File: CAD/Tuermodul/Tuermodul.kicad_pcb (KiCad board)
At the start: 2 copper layers, 160 x 100 mm, 95 parts, among them J101 Conn_02x16_Counter_Clockwise, Q201 Q_NPN_CBE, Q202 Q_NPN_CBE, Q203 Q_NPN_CBE, Q204 Q_NPN_CBE, Q205 Q_NPN_CBE, Q206 Q_NPN_CBE, Q207 Q_NPN_CBE, Q208 Q_NPN_CBE, Q209 Q_PMOS_GDS, Q210 Q_PMOS_GDS, Q211 Q_PMOS_GDS, Q212 Q_PMOS_GDS, Q213 Q_NPN_CBE, U101 93LC46B, U102 74HC595, U103 FT4232H, U104 MCP1825S, Y101 12MHz

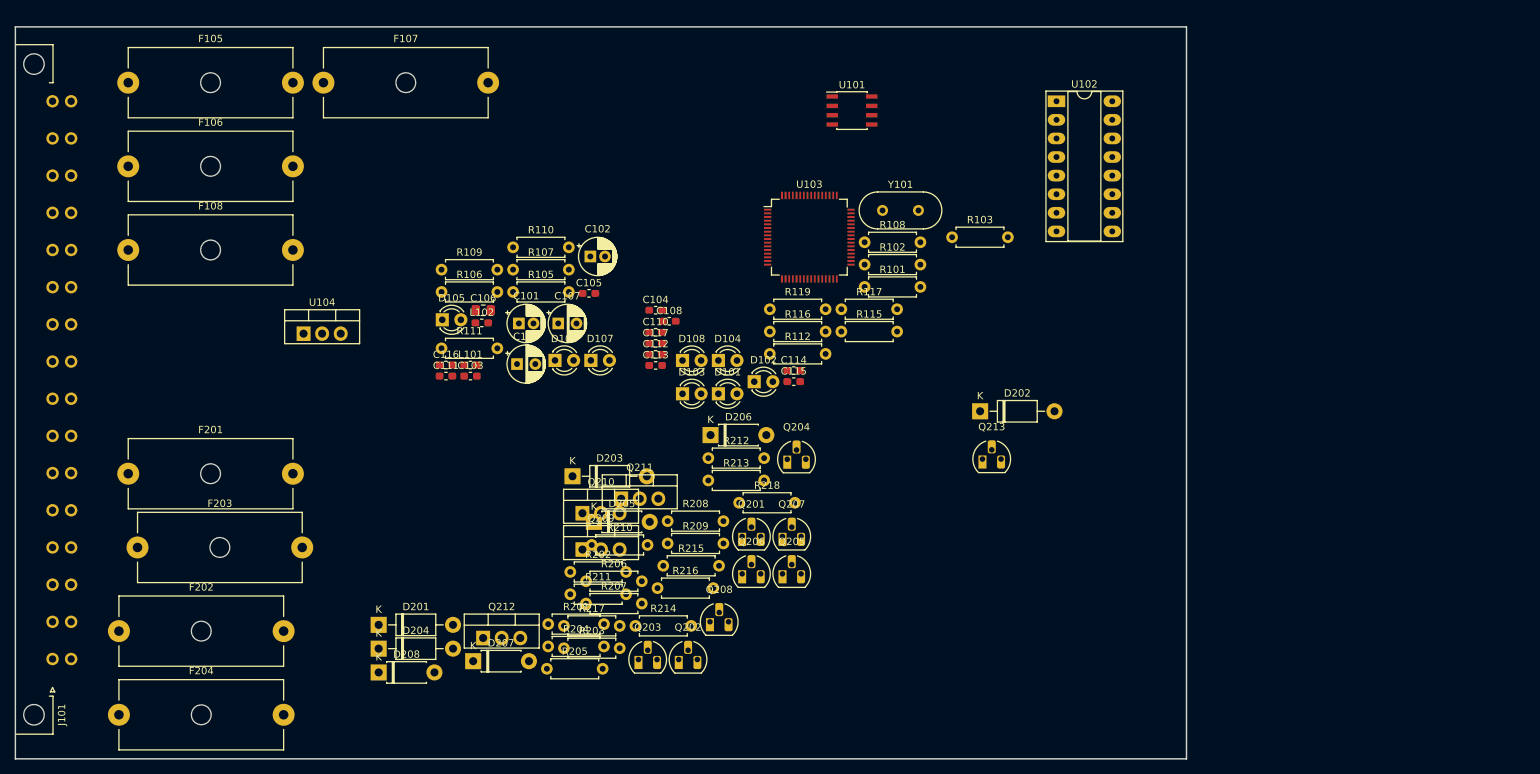
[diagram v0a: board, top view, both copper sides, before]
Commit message: -add: Fuse Error, missing LEDs -mod: some Resistor footprints changed -mod: first placement in layout
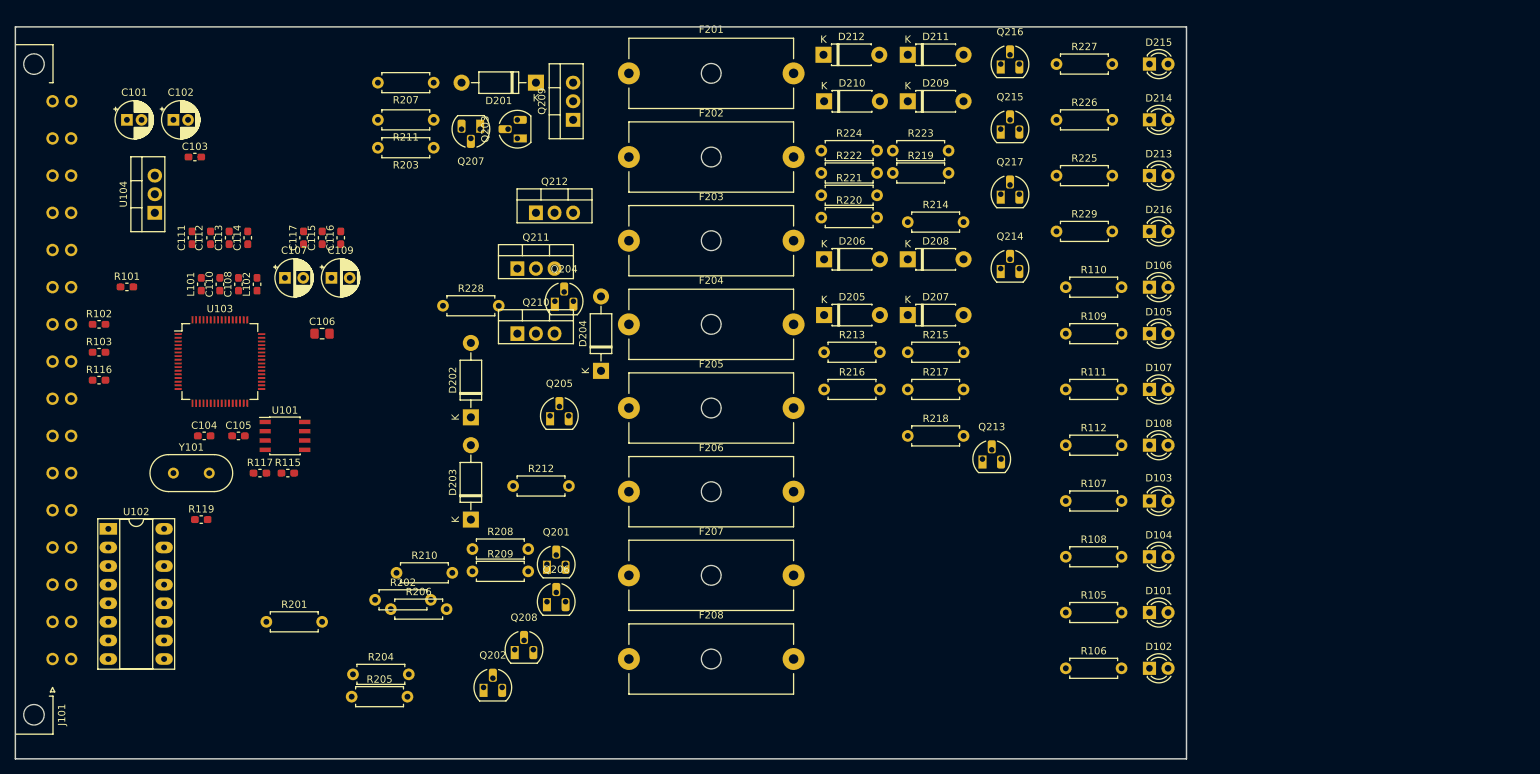
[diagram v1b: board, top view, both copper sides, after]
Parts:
- removed F105, F106, F107, F108: Fuse_Small, Fuse:Fuseholder_Cylinder-5x20mm_Schurter_0031_8201_Horizontal_Open
- added D209: 1N4148, Diode_THT:D_DO-41_SOD81_P7.62mm_Horizontal, F.Cu at (186.7, 54.6)
- added D210: 1N4148, Diode_THT:D_DO-41_SOD81_P7.62mm_Horizontal, F.Cu at (175.3, 54.6)
- added D211: 1N4148, Diode_THT:D_DO-41_SOD81_P7.62mm_Horizontal, F.Cu at (186.7, 48.3)
- added D212: 1N4148, Diode_THT:D_DO-41_SOD81_P7.62mm_Horizontal, F.Cu at (175.2, 48.3)
- added D213: rt, LED_THT:LED_D3.0mm, F.Cu at (219.7, 64.8)
- added D214: rt, LED_THT:LED_D3.0mm, F.Cu at (219.7, 57.1)
- added D215: rt, LED_THT:LED_D3.0mm, F.Cu at (219.7, 49.5)
- added D216: rt, LED_THT:LED_D3.0mm, F.Cu at (219.7, 72.4)
- added F205: 0.5A, Fuse:Fuseholder_Cylinder-5x20mm_Schurter_0031_8201_Horizontal_Open, F.Cu at (148.6, 96.5)
- added F206: 0.5A, Fuse:Fuseholder_Cylinder-5x20mm_Schurter_0031_8201_Horizontal_Open, F.Cu at (148.6, 108.0)
- added F207: 0.5A, Fuse:Fuseholder_Cylinder-5x20mm_Schurter_0031_8201_Horizontal_Open, F.Cu at (148.6, 119.4)
- added F208: 0.5A, Fuse:Fuseholder_Cylinder-5x20mm_Schurter_0031_8201_Horizontal_Open, F.Cu at (148.6, 130.8)
- added Q214: Q_NPN_CBE, Package_TO_SOT_THT:TO-92_HandSolder, F.Cu at (199.4, 77.5)
- added Q215: Q_NPN_CBE, Package_TO_SOT_THT:TO-92_HandSolder, F.Cu at (199.4, 58.4)
- added Q216: Q_NPN_CBE, Package_TO_SOT_THT:TO-92_HandSolder, F.Cu at (199.4, 49.5)
- added Q217: Q_NPN_CBE, Package_TO_SOT_THT:TO-92_HandSolder, F.Cu at (199.4, 67.3)
- added R219: 1M, Resistor_THT:R_Axial_DIN0207_L6.3mm_D2.5mm_P7.62mm_Horizontal, F.Cu at (184.6, 64.4)
- added R220: 10k, Resistor_THT:R_Axial_DIN0207_L6.3mm_D2.5mm_P7.62mm_Horizontal, F.Cu at (174.9, 70.5)
- added R221: 10k, Resistor_THT:R_Axial_DIN0207_L6.3mm_D2.5mm_P7.62mm_Horizontal, F.Cu at (174.9, 67.5)
- added R222: 10k, Resistor_THT:R_Axial_DIN0207_L6.3mm_D2.5mm_P7.62mm_Horizontal, F.Cu at (174.9, 64.4)
- added R223: 10k, Resistor_THT:R_Axial_DIN0207_L6.3mm_D2.5mm_P7.62mm_Horizontal, F.Cu at (184.6, 61.4)
- added R224: 10k, Resistor_THT:R_Axial_DIN0207_L6.3mm_D2.5mm_P7.62mm_Horizontal, F.Cu at (174.9, 61.4)
- added R225: 330R, Resistor_THT:R_Axial_DIN0207_L6.3mm_D2.5mm_P7.62mm_Horizontal, F.Cu at (207.0, 64.8)
- added R226: 330R, Resistor_THT:R_Axial_DIN0207_L6.3mm_D2.5mm_P7.62mm_Horizontal, F.Cu at (207.0, 57.1)
- added R227: 1k, Resistor_THT:R_Axial_DIN0207_L6.3mm_D2.5mm_P7.62mm_Horizontal, F.Cu at (207.0, 49.5)
- added R228: 10k, Resistor_THT:R_Axial_DIN0207_L6.3mm_D2.5mm_P7.62mm_Horizontal, F.Cu at (123.2, 82.5)
- added R229: 330R, Resistor_THT:R_Axial_DIN0207_L6.3mm_D2.5mm_P7.62mm_Horizontal, F.Cu at (207.0, 72.4)
- R101, R102, R103, R115, R116, R117, R119: footprint Resistor_THT:R_Axial_DIN0207_L6.3mm_D2.5mm_P7.62mm_Horizontal -> Resistor_SMD:R_0603_1608Metric_Pad1.05x0.95mm_HandSolder
- moved U102 142.1 mm to (77.5, 113.0)
- moved R103 117.6 mm to (76.2, 88.9)
- moved R102 104.9 mm to (76.2, 85.1)
- moved Y101 103.3 mm to (86.4, 105.4)
- moved R101 100.8 mm to (80.0, 80.0)
- moved R106 99.6 mm to (208.3, 132.1)
- moved D105 96.6 mm to (219.7, 86.4)
- moved F202 95.1 mm to (148.6, 62.2)
- moved R116 91.9 mm to (76.2, 92.7)
- moved D208 91.7 mm to (186.7, 76.2)
- moved U101 89.3 mm to (101.6, 100.3)
- moved F204 87.7 mm to (148.6, 85.1)
- moved F201 87.6 mm to (148.6, 50.8)
- moved R105 87.3 mm to (208.3, 124.5)
- moved R109 85.7 mm to (208.3, 86.4)
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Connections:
- Q213 pad 1: +12V -> Net-(Q213-Pad1)
- Q213 pad 3: Net-(Q213-Pad3) -> GND
- R218 pad 1: Net-(Q213-Pad3) -> +12V
- R218 pad 2: GND -> Net-(Q213-Pad1)

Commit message: -add: switch library for spdt switches -mod: improvements in schematic, bugfixes -mod: placement and routing of the ftdi chip + chicken food
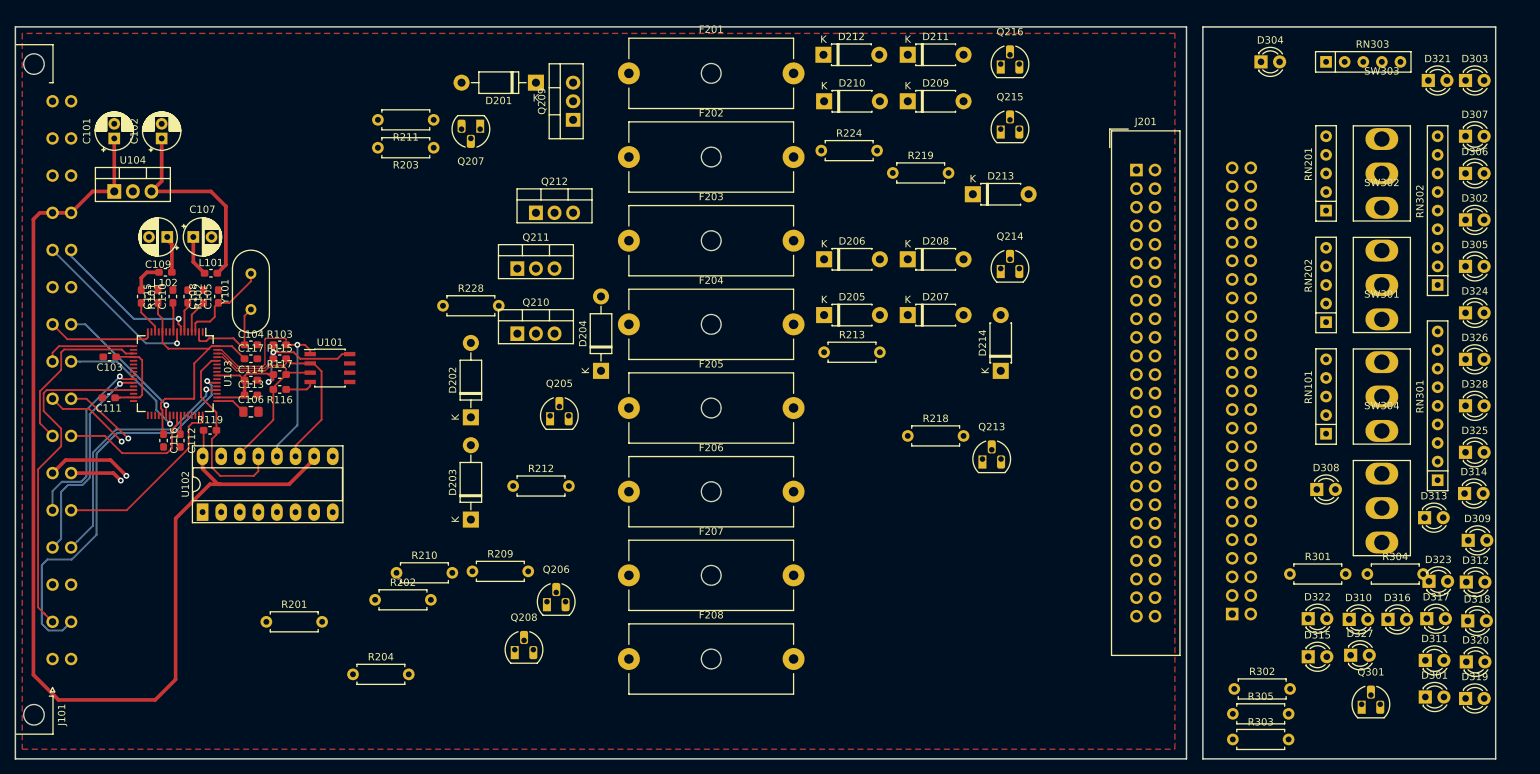
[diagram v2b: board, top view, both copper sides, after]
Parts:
- removed D101, D102, D103, D104, D105, D106, D107, D108, D215, D216: rt, LED_THT:LED_D3.0mm
- removed Q201, Q202, Q203, Q204, Q217: Q_NPN_CBE, Package_TO_SOT_THT:TO-92_HandSolder
- removed R105, R106, R107, R108, R109, R110, R111, R112, R225, R226, R229: 330R, Resistor_THT:R_Axial_DIN0207_L6.3mm_D2.5mm_P7.62mm_Horizontal
- removed R205, R206, R207, R208: 100k, Resistor_THT:R_Axial_DIN0207_L6.3mm_D2.5mm_P7.62mm_Horizontal
- removed R214, R215, R216, R217, R220, R221, R222, R223: 10k, Resistor_THT:R_Axial_DIN0207_L6.3mm_D2.5mm_P7.62mm_Horizontal
- removed R227: 1k, Resistor_THT:R_Axial_DIN0207_L6.3mm_D2.5mm_P7.62mm_Horizontal
- added D301: rt, LED_THT:LED_D3.0mm, F.Cu at (257.4, 136.0)
- added D302: rt, LED_THT:LED_D3.0mm, F.Cu at (262.9, 70.8)
- added D303: rt, LED_THT:LED_D3.0mm, F.Cu at (262.9, 51.8)
- added D304: rt, LED_THT:LED_D3.0mm, F.Cu at (234.9, 49.2)
- added D305: rt, LED_THT:LED_D3.0mm, F.Cu at (262.9, 77.2)
- added D306: gn, LED_THT:LED_D3.0mm, F.Cu at (262.9, 64.5)
- added D307: rt, LED_THT:LED_D3.0mm, F.Cu at (262.9, 59.4)
- added D308: rt, LED_THT:LED_D3.0mm, F.Cu at (242.6, 107.7)
- added D309: rt, LED_THT:LED_D3.0mm, F.Cu at (263.3, 114.6)
- added D310: gn, LED_THT:LED_D3.0mm, F.Cu at (247.0, 125.4)
- added D311: rt, LED_THT:LED_D3.0mm, F.Cu at (257.4, 131.0)
- added D312: rt, LED_THT:LED_D3.0mm, F.Cu at (263.0, 120.3)
- added D313: rt, LED_THT:LED_D3.0mm, F.Cu at (257.3, 111.5)
- added D314: gn, LED_THT:LED_D3.0mm, F.Cu at (262.8, 108.2)
- added D315: rt, LED_THT:LED_D3.0mm, F.Cu at (241.4, 130.5)
- added D316: rt, LED_THT:LED_D3.0mm, F.Cu at (252.3, 125.4)
- added D317: rt, LED_THT:LED_D3.0mm, F.Cu at (257.6, 125.3)
- added D318: gn, LED_THT:LED_D3.0mm, F.Cu at (263.2, 125.6)
- added D319: rt, LED_THT:LED_D3.0mm, F.Cu at (262.9, 136.2)
- added D320: rt, LED_THT:LED_D3.0mm, F.Cu at (263.0, 131.2)
- added D321: rt, LED_THT:LED_D3.0mm, F.Cu at (257.8, 51.8)
- added D322: rt, LED_THT:LED_D3.0mm, F.Cu at (241.4, 125.3)
- added D323: rt, LED_THT:LED_D3.0mm, F.Cu at (257.9, 120.2)
- added D324: rt, LED_THT:LED_D3.0mm, F.Cu at (262.9, 83.5)
- added D325: rt, LED_THT:LED_D3.0mm, F.Cu at (262.9, 102.6)
- added D326: rt, LED_THT:LED_D3.0mm, F.Cu at (262.9, 89.9)
- added D327: rt, LED_THT:LED_D3.0mm, F.Cu at (247.2, 130.3)
- added D328: rt, LED_THT:LED_D3.0mm, F.Cu at (262.9, 96.2)
- added J201: Conn_02x25_Counter_Clockwise, Connector_IDC:IDC-Header_2x25_P2.54mm_Vertical, F.Cu at (217.9, 64.0)
- added J301: Conn_02x25_Counter_Clockwise, Connector_IDC:IDC-Header_2x25_P2.54mm_Vertical, B.Cu at (231.0, 124.7)
- added Q301: Q_NPN_CBE, Package_TO_SOT_THT:TO-92_HandSolder, F.Cu at (248.7, 137.0)
- added R301: 1k, Resistor_THT:R_Axial_DIN0207_L6.3mm_D2.5mm_P7.62mm_Horizontal, F.Cu at (238.9, 119.2)
- added R302: 330R, Resistor_THT:R_Axial_DIN0207_L6.3mm_D2.5mm_P7.62mm_Horizontal, F.Cu at (231.3, 134.9)
- added R303: 330R, Resistor_THT:R_Axial_DIN0207_L6.3mm_D2.5mm_P7.62mm_Horizontal, F.Cu at (231.1, 141.8)
- added R304: 330R, Resistor_THT:R_Axial_DIN0207_L6.3mm_D2.5mm_P7.62mm_Horizontal, F.Cu at (249.5, 119.2)
- added R305: 1k, Resistor_THT:R_Axial_DIN0207_L6.3mm_D2.5mm_P7.62mm_Horizontal, F.Cu at (231.1, 138.3)
- added RN101: 2k7, Resistor_THT:R_Array_SIP5, F.Cu at (243.8, 100.0)
- added RN201: 4x10k, Resistor_THT:R_Array_SIP5, F.Cu at (243.8, 69.5)
- added RN202: 4x10k, Resistor_THT:R_Array_SIP5, F.Cu at (243.8, 84.8)
- added RN301: 8x2k7, Resistor_THT:R_Array_SIP9, F.Cu at (259.1, 106.4)
- added RN302: 8x10k, Resistor_THT:R_Array_SIP9, F.Cu at (259.1, 79.7)
- added RN303: 4x2k7, Resistor_THT:R_Array_SIP5, F.Cu at (243.8, 49.2)
- added SW301: SW_SPDT_MSM, Switches:SPDT, F.Cu at (251.5, 95.0)
- added SW302: SW_SPDT_MSM, Switches:SPDT, F.Cu at (251.5, 79.7)
- added SW303: SW_SPDT_MSM, Switches:SPDT, F.Cu at (251.5, 64.5)
- added SW304: SW_SPDT_MSM, Switches:SPDT, F.Cu at (251.5, 110.2)
- D213, D214: value rt -> 1N4148; footprint LED_THT:LED_D3.0mm -> Diode_THT:D_DO-41_SOD81_P7.62mm_Horizontal
- moved D214 39.9 mm to (199.4, 91.4), turned to 90 degrees
- moved C116 36.8 mm to (85.0, 101.0), turned to 270 degrees
- moved C103 29.7 mm to (77.6, 89.5), turned to 180 degrees
- moved C112 28.0 mm to (87.3, 101.0), turned to 270 degrees
- moved Y101 24.7 mm to (97.0, 83.1), turned to 90 degrees
- moved R116 24.7 mm to (100.9, 94.0), turned to 180 degrees
- moved R103 24.7 mm to (100.9, 87.9)
- moved C111 24.6 mm to (77.5, 95.1), turned to 180 degrees
- moved D213 24.3 mm to (195.6, 67.3)
- moved C115 23.8 mm to (84.3, 81.3)
- moved C109 23.1 mm to (85.5, 73.2), turned to 180 degrees
- moved C113 21.7 mm to (97.0, 94.7), turned to 0 degrees
- moved C114 19.5 mm to (97.0, 92.7), turned to 0 degrees
- moved C105 19.2 mm to (92.5, 81.3), turned to 90 degrees
- moved C117 18.0 mm to (97.0, 89.8), turned to 0 degrees
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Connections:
- C106 pad 1: Net-(C106-Pad1) -> +1V8
- D213 pad 1: GND -> Net-(D213-Pad1)
- D213 pad 2: Net-(D213-Pad2) -> Net-(D209-Pad2)
- D214 pad 1: GND -> Net-(D214-Pad1)
- D214 pad 2: Net-(D214-Pad2) -> Net-(D205-Pad2)
- Q205 pad 2: Net-(Q201-Pad1) -> Net-(Q205-Pad2)
- Q206 pad 2: Net-(Q202-Pad1) -> Net-(Q206-Pad2)
- Q207 pad 2: Net-(Q203-Pad1) -> Net-(Q207-Pad2)
- Q208 pad 2: Net-(Q204-Pad1) -> Net-(Q208-Pad2)
- Q209 pad 3: /DoorA_Lock -> /Peripherie/DoorA_Auto
- Q210 pad 3: /DoorB_Lock -> /Peripherie/DoorB_Auto
- Q211 pad 3: /DoorC_Lock -> /Peripherie/DoorC_Auto
- Q212 pad 3: /DoorD_Lock -> /Peripherie/DoorD_Auto
- Q213 pad 2: Net-(D205-Pad2) -> Net-(D214-Pad1)
- Q214 pad 2: Net-(D209-Pad2) -> Net-(D213-Pad1)
- R201 pad 1: Net-(Q201-Pad2) -> Net-(Q205-Pad2)
- R202 pad 1: Net-(Q202-Pad2) -> Net-(Q206-Pad2)
- R203 pad 1: Net-(Q203-Pad2) -> Net-(Q207-Pad2)
- R204 pad 1: Net-(Q204-Pad2) -> Net-(Q208-Pad2)
- U101 pad 6: Net-(U101-Pad6) -> (no net)
- U101 pad 7: Net-(U101-Pad7) -> (no net)
- U102 pad 1: Net-(R106-Pad1) -> /DA_Rx
- U102 pad 15: Net-(R105-Pad1) -> /DA_Tx
- U102 pad 2: Net-(R107-Pad1) -> /DB_Tx
- U102 pad 3: Net-(R108-Pad1) -> /DB_Rx
- U102 pad 4: Net-(R109-Pad1) -> /DC_Tx
- U102 pad 5: Net-(R110-Pad1) -> /DC_Rx
- U102 pad 6: Net-(R111-Pad1) -> /DD_Tx
- U102 pad 7: Net-(R112-Pad1) -> /DD_Rx
- U102 pad 9: Net-(U102-Pad9) -> (no net)
- U103 pad 12: Net-(C106-Pad1) -> +1V8
- U103 pad 19: Net-(U103-Pad19) -> /DoorA_MK
- U103 pad 20: Net-(U103-Pad20) -> +3V3
- U103 pad 21: Net-(U103-Pad21) -> (no net)
- U103 pad 22: Net-(U103-Pad22) -> (no net)
- U103 pad 23: Net-(U103-Pad23) -> (no net)
- U103 pad 24: Net-(U103-Pad24) -> (no net)
- U103 pad 29: Net-(U103-Pad29) -> /DoorB_MK
- U103 pad 30: Net-(U103-Pad30) -> (no net)
- U103 pad 31: Net-(U103-Pad20) -> +3V3
- U103 pad 32: Net-(U103-Pad32) -> (no net)
- U103 pad 33: Net-(U103-Pad33) -> (no net)
- U103 pad 34: Net-(U103-Pad34) -> (no net)
- U103 pad 36: Net-(U103-Pad36) -> (no net)
- U103 pad 37: Net-(C106-Pad1) -> +1V8
- U103 pad 41: Net-(U103-Pad41) -> /DoorC_MK
- U103 pad 42: Net-(U103-Pad20) -> +3V3
- U103 pad 43: Net-(U103-Pad43) -> (no net)
- U103 pad 44: Net-(U103-Pad44) -> (no net)
- U103 pad 45: Net-(U103-Pad45) -> (no net)
- U103 pad 46: Net-(U103-Pad46) -> (no net)
- U103 pad 49: Net-(C106-Pad1) -> +1V8
- U103 pad 54: Net-(U103-Pad54) -> /DoorD_MK
- U103 pad 55: Net-(U103-Pad55) -> (no net)
- U103 pad 56: Net-(U103-Pad20) -> +3V3
- U103 pad 57: Net-(U103-Pad57) -> (no net)
- U103 pad 58: Net-(U103-Pad58) -> (no net)
- U103 pad 59: Net-(U103-Pad59) -> (no net)
- U103 pad 64: Net-(C106-Pad1) -> +1V8
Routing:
- net +5V: track 0.00 -> 157.4 mm
- net +3V3: track 0.00 -> 81.3 mm, vias 0 -> 2
- net /DoorD_MK: track 0.00 -> 55.8 mm, vias 0 -> 1
- net /DoorB_MK: track 0.00 -> 47.0 mm
- net +1V8: track 0.00 -> 39.2 mm
- net /EECS: track 0.00 -> 35.3 mm, vias 0 -> 1
- net /DoorD_RX_DTE: track 0.00 -> 35.2 mm, vias 0 -> 1
- net /DoorB_RX_DTE: track 0.00 -> 30.2 mm, vias 0 -> 1
- net /EECLK: track 0.00 -> 29.9 mm
- net /EEDATA: track 0.00 -> 28.5 mm
- net /~PWREN~: track 0.00 -> 26.2 mm
- net /DoorB_TX_DTE: track 0.00 -> 25.6 mm, vias 0 -> 1
- net /DoorD_TX_DTE: track 0.00 -> 25.5 mm
- net /D+: track 0.00 -> 23.9 mm, vias 0 -> 1
- net /DoorA_MK: track 0.00 -> 23.6 mm
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- added copper zone on F.Cu, net GND
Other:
- board size 160 x 100 mm -> 202.2 x 100 mm
- rule trace_min: 0.2 -> 0.05
